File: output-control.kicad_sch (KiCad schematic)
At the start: 57 parts

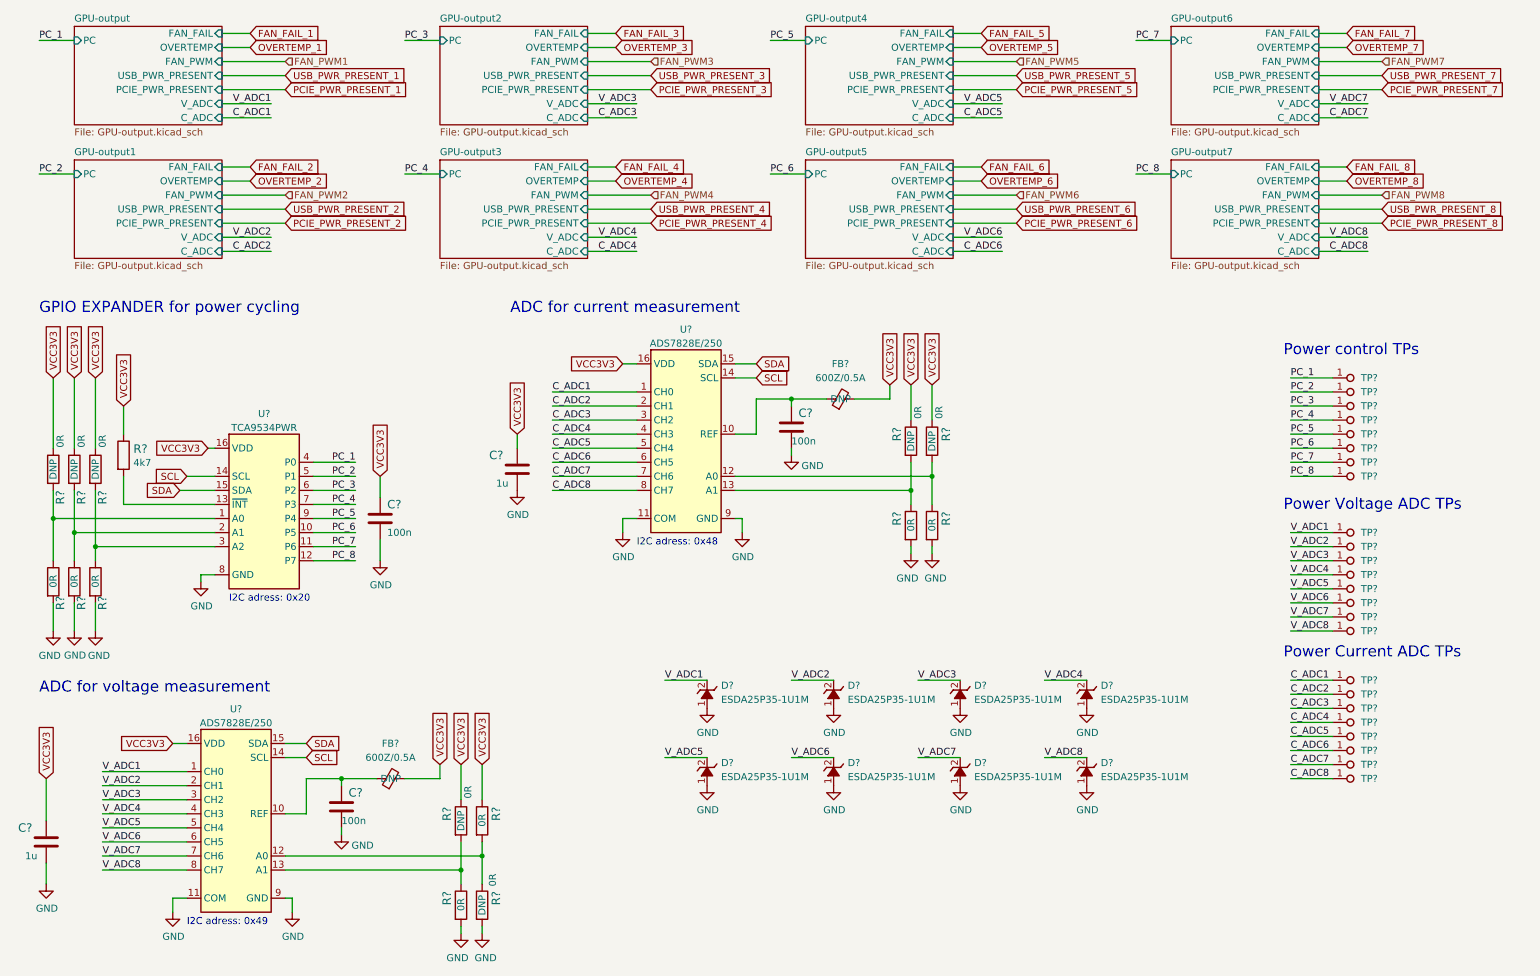
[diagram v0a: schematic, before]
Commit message: Change power flags on schematic
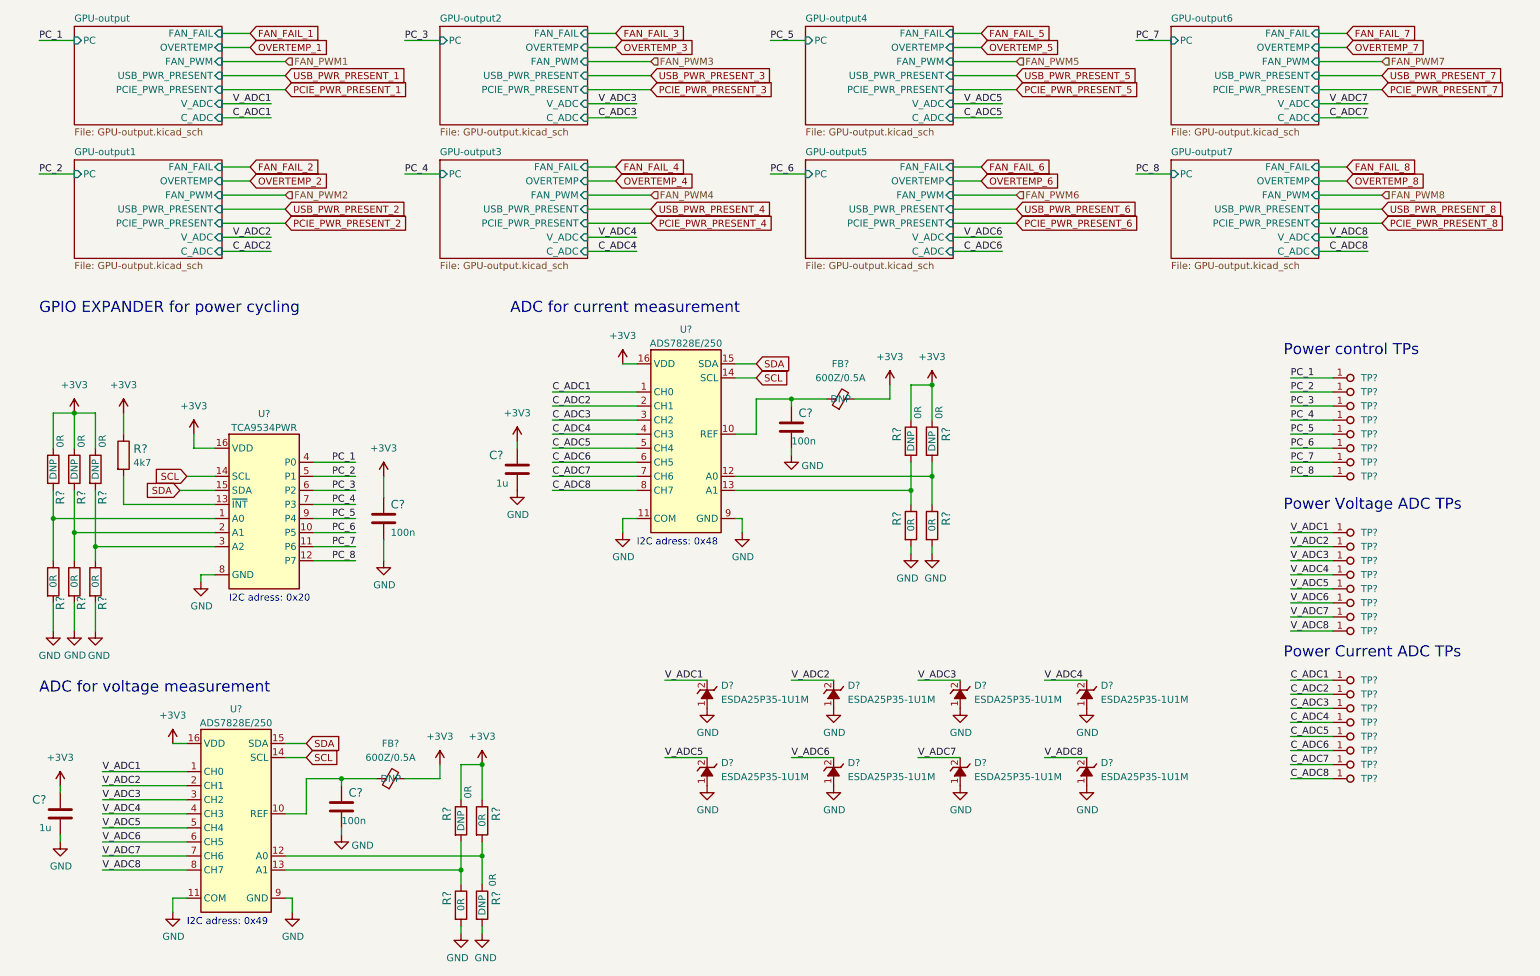
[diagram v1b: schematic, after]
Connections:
- net VCC3V3 renamed +3V3
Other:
- moved on the sheet: C?

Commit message: Reannotate schematic symbols
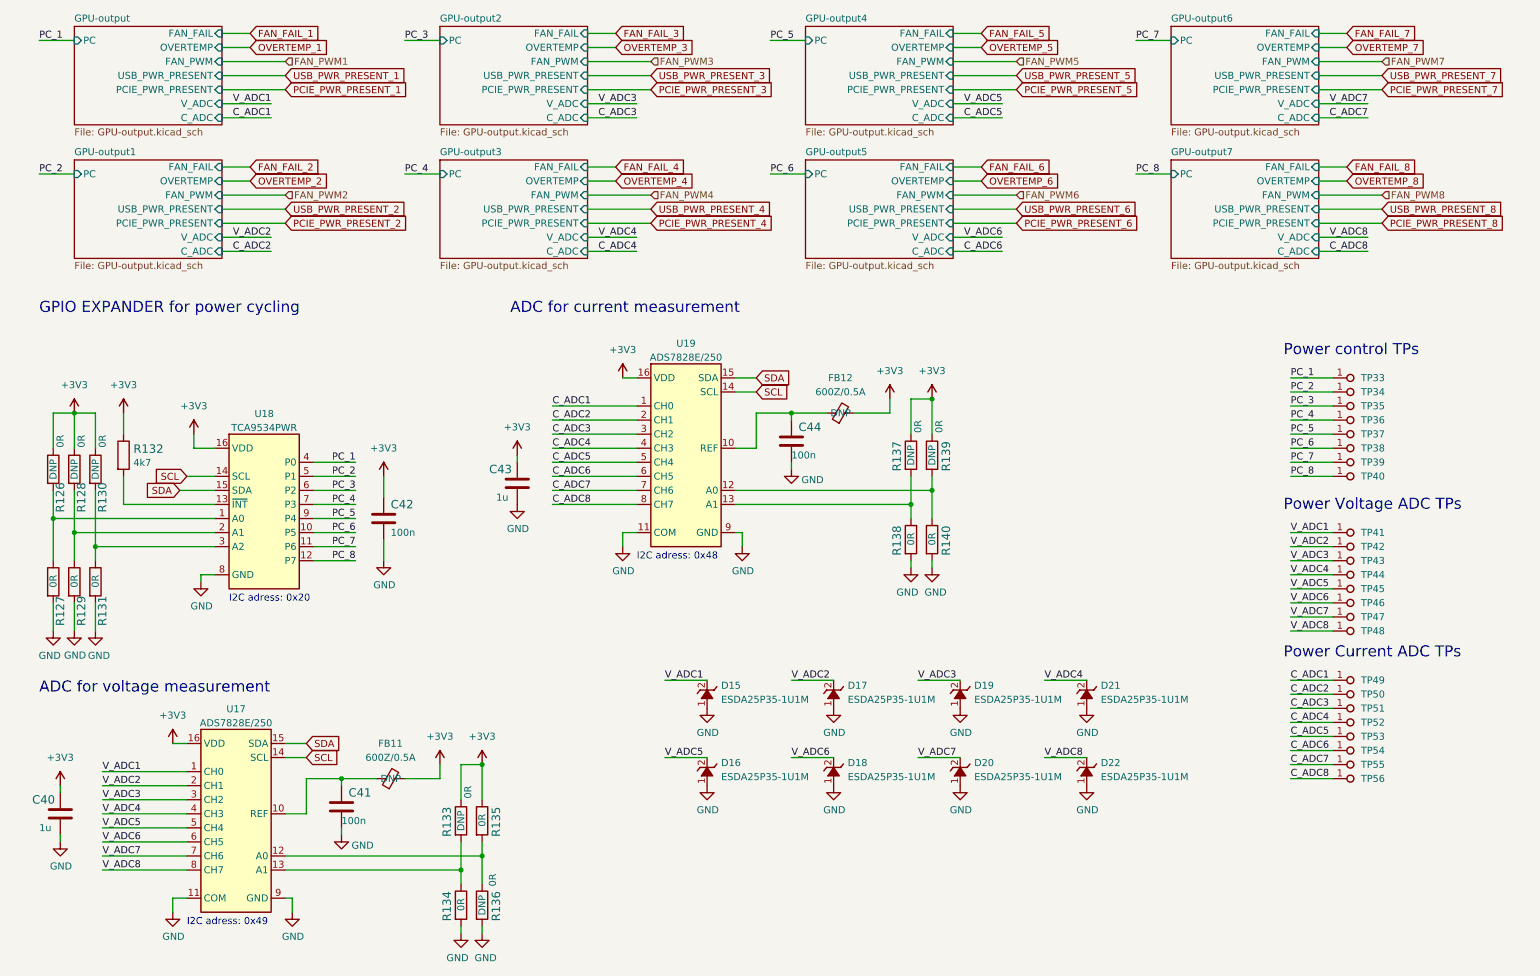
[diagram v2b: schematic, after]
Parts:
- gave numbers to parts that had none: 57
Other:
- moved on the sheet: C43, C44, FB12, R137, R138, R139, R140, U19

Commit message: Set resitsors to standard
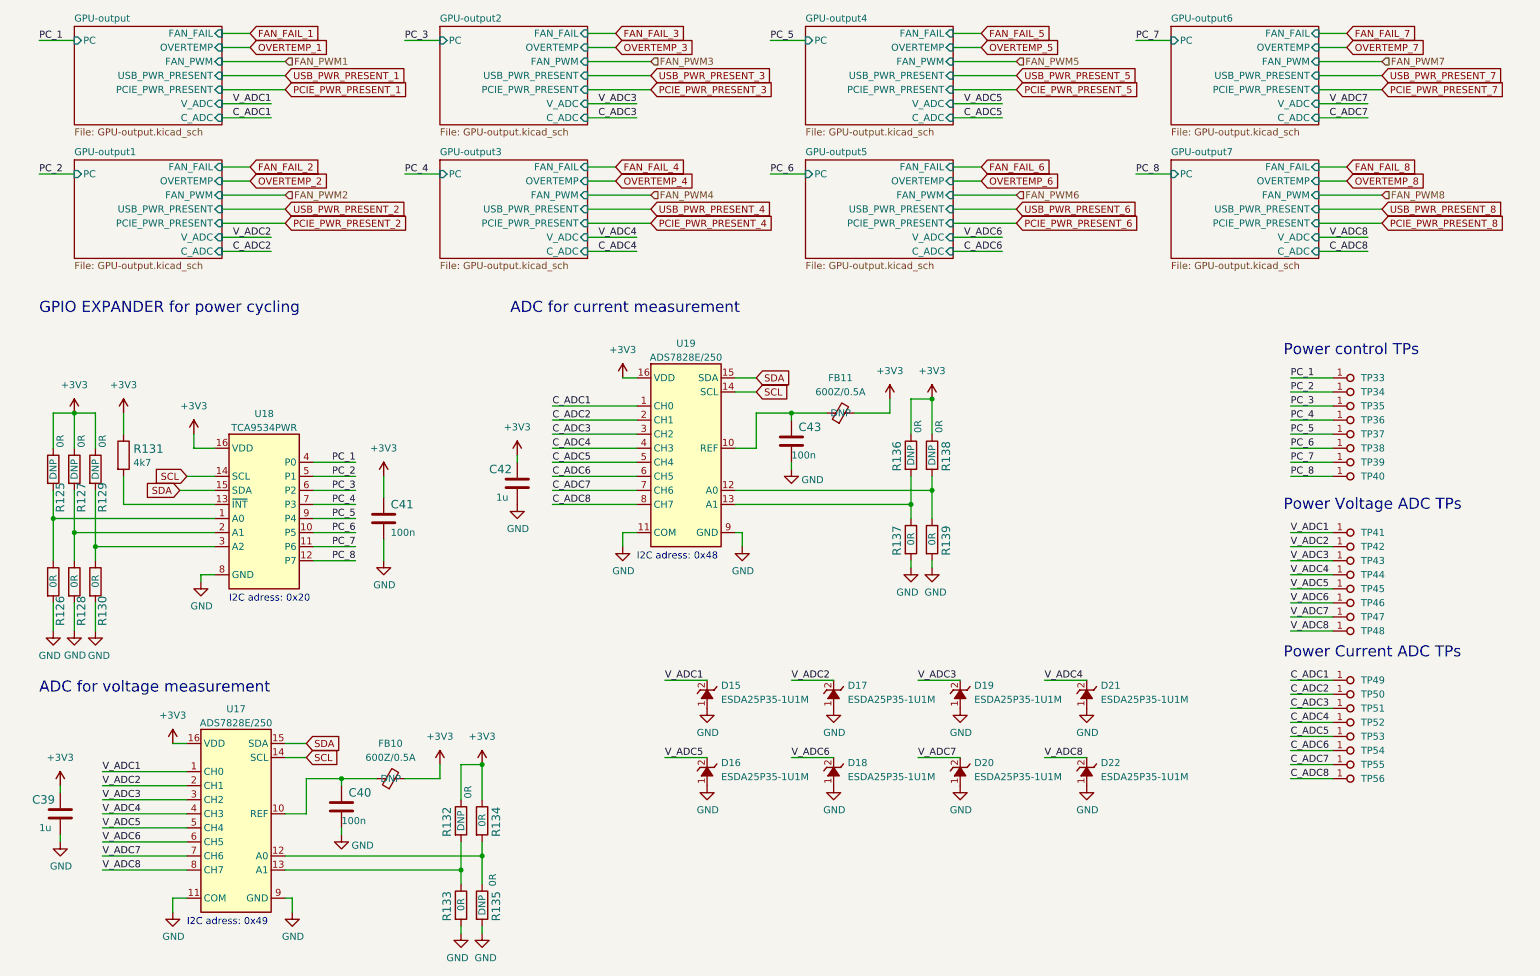
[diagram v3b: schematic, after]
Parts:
- renumbered C40 to C39, C41 to C40, C42 to C41, C43 to C42, C44 to C43, FB11 to FB10, FB12 to FB11, R126 to R125, R127 to R126, R128 to R127, R129 to R128, R130 to R129, R131 to R130, R132 to R131, R133 to R132, R134 to R133, R135 to R134, R136 to R135, R137 to R136, R138 to R137, R139 to R138, R140 to R139
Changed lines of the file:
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@@
   (symbol (lib_id "antmicroResistors0402:R_0R_0402") (at 17.78 97.79 270) (unit 1)
     (in_bom yes) (on_board yes)
-    (property "Reference" "R126" (id 0) (at 19.05 102.87 0)
+    (property "Reference" "R125" (id 0) (at 19.05 102.87 0)
       (effects (font (size 1.524 1.524)))
     )
@@
   (symbol (lib_id "antmicroResistors0402:R_0R_0402") (at 95.25 161.29 270) (unit 1)
     (in_bom yes) (on_board yes)
-    (property "Reference" "R135" (id 0) (at 97.79 158.75 0)
+    (property "Reference" "R134" (id 0) (at 97.79 158.75 0)
       (effects (font (size 1.524 1.524)) (justify left))
     )
@@
   (symbol (lib_id "antmicroResistors0402:R_4k7_0402") (at 30.48 95.25 270) (unit 1)
     (in_bom yes) (on_board yes)
-    (property "Reference" "R132" (id 0) (at 32.258 94.107 90)
+    (property "Reference" "R131" (id 0) (at 32.258 94.107 90)
       (effects (font (size 1.524 1.524)) (justify left))
     )
@@
   (symbol (lib_id "antmicroResistors0402:R_0R_0402") (at 21.59 118.11 270) (unit 1)
     (in_bom yes) (on_board yes)
-    (property "Reference" "R129" (id 0) (at 22.86 120.65 0)
+    (property "Reference" "R128" (id 0) (at 22.86 120.65 0)
       (effects (font (size 1.524 1.524)) (justify left))
     )
@@
   (symbol (lib_id "antmicroResistors0402:R_0R_0402") (at 176.53 95.25 270) (unit 1)
     (in_bom yes) (on_board yes)
-    (property "Reference" "R139" (id 0) (at 179.07 92.71 0)
+    (property "Reference" "R138" (id 0) (at 179.07 92.71 0)
       (effects (font (size 1.524 1.524)) (justify left))
     )
@@
   (symbol (lib_id "antmicroFerriteBeadsandChips:FB_600Z_0.5A_Murata-BLM18AG_0603") (at 157.48 87.63 0) (unit 1)
     (in_bom yes) (on_board yes)
-    (property "Reference" "FB12" (id 0) (at 159.9819 81.28 0)
+    (property "Reference" "FB11" (id 0) (at 159.9819 81.28 0)
       (effects (font (size 1.27 1.27) (thickness 0.15)))
     )
@@
   (symbol (lib_id "antmicroCapacitors0402:C_1u_0402") (at 19.05 160.02 0) (unit 1)
     (in_bom yes) (on_board yes)
-    (property "Reference" "C40" (id 0) (at 13.97 157.48 0)
+    (property "Reference" "C39" (id 0) (at 13.97 157.48 0)
       (effects (font (size 1.524 1.524)) (justify left))
     )
@@
   (symbol (lib_id "antmicroFerriteBeadsandChips:FB_600Z_0.5A_Murata-BLM18AG_0603") (at 76.2 153.67 0) (unit 1)
     (in_bom yes) (on_board yes)
-    (property "Reference" "FB11" (id 0) (at 78.7019 147.32 0)
+    (property "Reference" "FB10" (id 0) (at 78.7019 147.32 0)
       (effects (font (size 1.27 1.27) (thickness 0.15)))
     )
@@
   (symbol (lib_id "antmicroResistors0402:R_0R_0402") (at 91.44 161.29 270) (unit 1)
     (in_bom yes) (on_board yes)
-    (property "Reference" "R133" (id 0) (at 88.9 158.75 0)
+    (property "Reference" "R132" (id 0) (at 88.9 158.75 0)
       (effects (font (size 1.524 1.524)) (justify left))
     )
@@
   (symbol (lib_id "antmicroResistors0402:R_0R_0402") (at 91.44 176.53 270) (unit 1)
     (in_bom yes) (on_board yes)
-    (property "Reference" "R134" (id 0) (at 88.9 173.99 0)
+    (property "Reference" "R133" (id 0) (at 88.9 173.99 0)
       (effects (font (size 1.524 1.524)) (justify left))
     )
@@
   (symbol (lib_id "antmicroResistors0402:R_0R_0402") (at 176.53 110.49 270) (unit 1)
     (in_bom yes) (on_board yes)
-    (property "Reference" "R140" (id 0) (at 179.07 107.95 0)
+    (property "Reference" "R139" (id 0) (at 179.07 107.95 0)
       (effects (font (size 1.524 1.524)) (justify left))
     )
@@
   (symbol (lib_id "antmicroCapacitors0402:C_100n_0402") (at 151.13 92.71 0) (unit 1)
     (in_bom yes) (on_board yes)
-    (property "Reference" "C44" (id 0) (at 152.4 90.17 0)
+    (property "Reference" "C43" (id 0) (at 152.4 90.17 0)
       (effects (font (size 1.524 1.524)) (justify left))
     )
@@
   (symbol (lib_id "antmicroResistors0402:R_0R_0402") (at 95.25 176.53 270) (unit 1)
     (in_bom yes) (on_board yes)
-    (property "Reference" "R136" (id 0) (at 97.79 173.99 0)
+    (property "Reference" "R135" (id 0) (at 97.79 173.99 0)
       (effects (font (size 1.524 1.524)) (justify left))
     )
@@
   (symbol (lib_id "antmicroResistors0402:R_0R_0402") (at 25.4 97.79 270) (unit 1)
     (in_bom yes) (on_board yes)
-    (property "Reference" "R130" (id 0) (at 26.67 102.87 0)
+    (property "Reference" "R129" (id 0) (at 26.67 102.87 0)
       (effects (font (size 1.524 1.524)))
     )
@@
   (symbol (lib_id "antmicroCapacitors0402:C_100n_0402") (at 69.85 158.75 0) (unit 1)
     (in_bom yes) (on_board yes)
-    (property "Reference" "C41" (id 0) (at 71.12 156.21 0)
+    (property "Reference" "C40" (id 0) (at 71.12 156.21 0)
       (effects (font (size 1.524 1.524)) (justify left))
     )
@@
   (symbol (lib_id "antmicroResistors0402:R_0R_0402") (at 172.72 110.49 270) (unit 1)
     (in_bom yes) (on_board yes)
-    (property "Reference" "R138" (id 0) (at 170.18 107.95 0)
+    (property "Reference" "R137" (id 0) (at 170.18 107.95 0)
       (effects (font (size 1.524 1.524)) (justify left))
     )
@@
   (symbol (lib_id "antmicroResistors0402:R_0R_0402") (at 21.59 97.79 270) (unit 1)
     (in_bom yes) (on_board yes)
-    (property "Reference" "R128" (id 0) (at 22.86 102.87 0)
+    (property "Reference" "R127" (id 0) (at 22.86 102.87 0)
       (effects (font (size 1.524 1.524)))
     )
@@
   (symbol (lib_id "antmicroCapacitors0402:C_1u_0402") (at 101.6 100.33 0) (unit 1)
     (in_bom yes) (on_board yes)
-    (property "Reference" "C43" (id 0) (at 96.52 97.79 0)
+    (property "Reference" "C42" (id 0) (at 96.52 97.79 0)
       (effects (font (size 1.524 1.524)) (justify left))
     )
@@
   (symbol (lib_id "antmicroResistors0402:R_0R_0402") (at 17.78 118.11 270) (unit 1)
     (in_bom yes) (on_board yes)
-    (property "Reference" "R127" (id 0) (at 19.05 120.65 0)
+    (property "Reference" "R126" (id 0) (at 19.05 120.65 0)
       (effects (font (size 1.524 1.524)) (justify left))
     )
@@
   (symbol (lib_id "antmicroResistors0402:R_0R_0402") (at 172.72 95.25 270) (unit 1)
     (in_bom yes) (on_board yes)
-    (property "Reference" "R137" (id 0) (at 170.18 92.71 0)
+    (property "Reference" "R136" (id 0) (at 170.18 92.71 0)
       (effects (font (size 1.524 1.524)) (justify left))
     )
@@
   (symbol (lib_id "antmicroCapacitors0402:C_100n_0402") (at 77.47 106.68 0) (unit 1)
     (in_bom yes) (on_board yes)
-    (property "Reference" "C42" (id 0) (at 78.74 104.14 0)
+    (property "Reference" "C41" (id 0) (at 78.74 104.14 0)
       (effects (font (size 1.524 1.524)) (justify left))
     )
@@
   (symbol (lib_id "antmicroResistors0402:R_0R_0402") (at 25.4 118.11 270) (unit 1)
     (in_bom yes) (on_board yes)
-    (property "Reference" "R131" (id 0) (at 26.67 120.65 0)
+    (property "Reference" "R130" (id 0) (at 26.67 120.65 0)
       (effects (font (size 1.524 1.524)) (justify left))
     )

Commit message: Repleace non standard components in connectors and ftdi and power
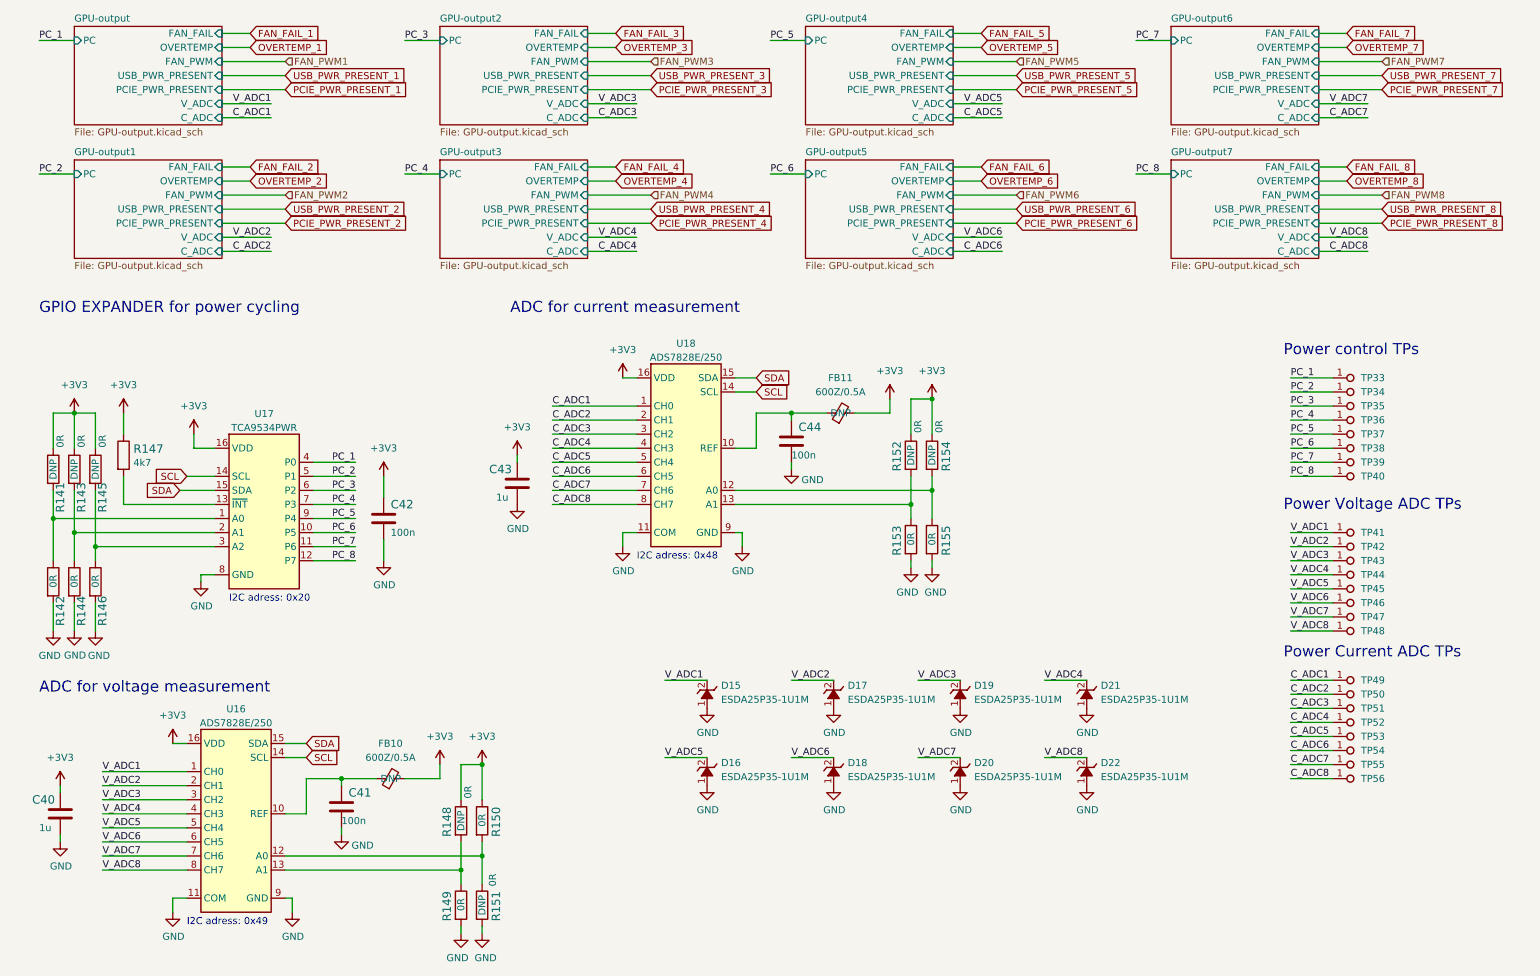
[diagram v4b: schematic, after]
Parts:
- renumbered C39 to C40, C40 to C41, C41 to C42, C42 to C43, C43 to C44, R125 to R141, R126 to R142, R127 to R143, R128 to R144, R129 to R145, R130 to R146, R131 to R147, R132 to R148, R133 to R149, R134 to R150, R135 to R151, R136 to R152, R137 to R153, R138 to R154, R139 to R155, U17 to U16, U18 to U17, U19 to U18
